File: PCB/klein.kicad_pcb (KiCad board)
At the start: 2 copper layers, 147.9 x 97.2 mm, 86 parts, among them J1 Conn_01x12, J2 Haptic Buzz, J3 Conn_01x04, J5 OLED-128x64, SW1 MX_SW_HS, SW10 MX_SW_HS, SW11 MX_SW_HS, SW12 MX_SW_HS, SW13 MX_SW_HS, SW14 MX_SW_HS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

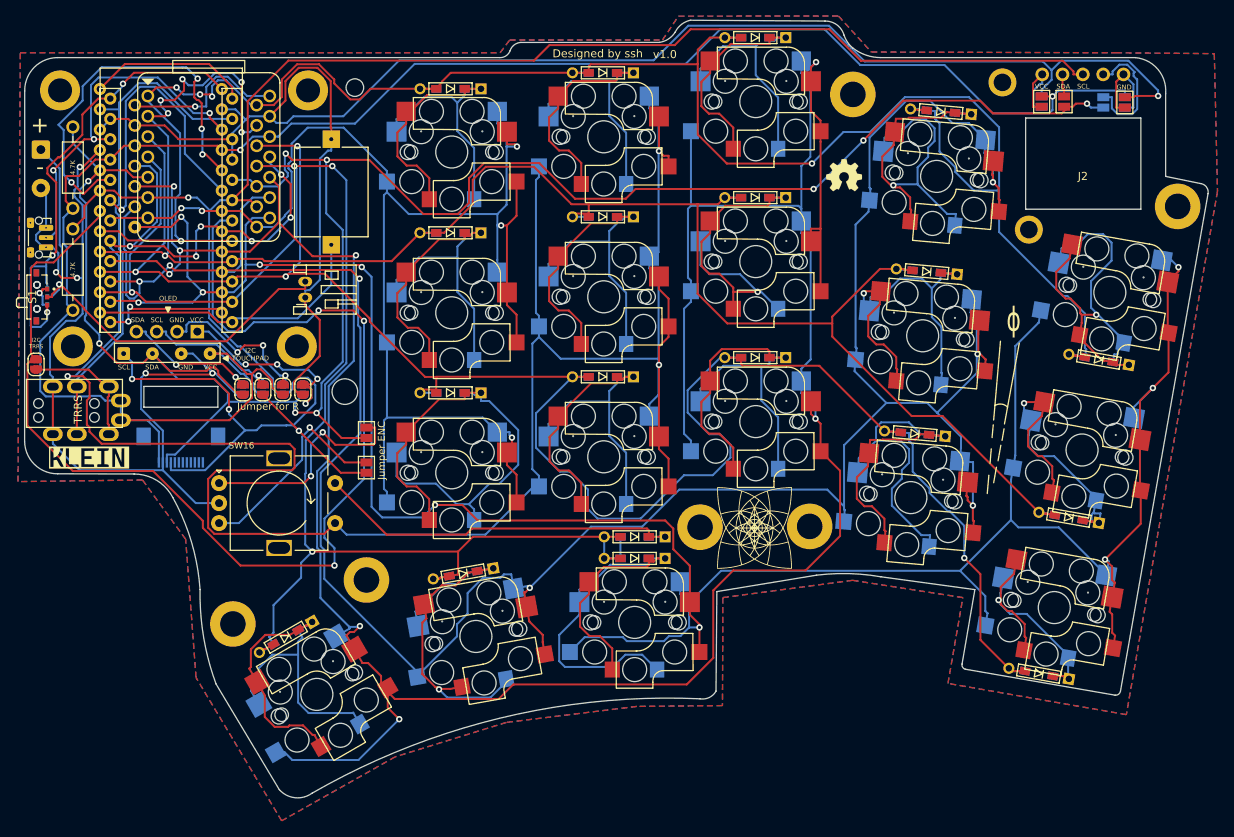
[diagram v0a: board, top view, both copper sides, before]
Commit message: Fix PCB Encoder Routes (Typo in Schematic) and IBOM project name fix
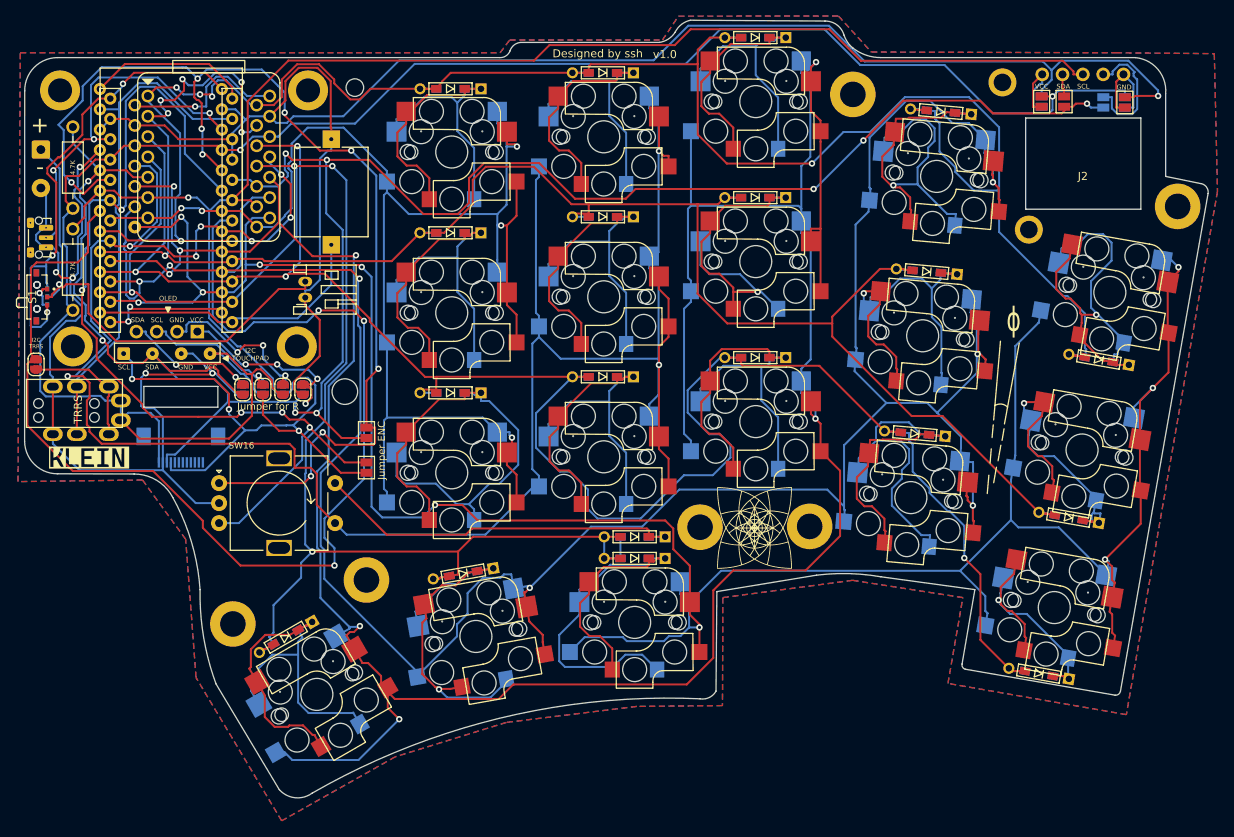
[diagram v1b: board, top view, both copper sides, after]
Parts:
- removed REF01, REF02: OSHW-Logo_5.7x6mm_SilkScreen, Symbol:OSHW-Logo_5.7x6mm_SilkScreen
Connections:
- U2 pad 19: ENCB -> ENC_B
- U2 pad 20: ENCA -> ENC_A
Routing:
- net ENC_A: track 28.2 -> 139.9 mm, vias 2 -> 9
- net ENC_B: track 27.0 -> 117.9 mm, vias 1 -> 5
- net ENCA: track 49.5 -> 0.00 mm, vias 4 -> 0
- net ENCB: track 36.6 -> 0.00 mm, vias 1 -> 0
- net COL 1: track 307.8 -> 286.5 mm
- net VCC_3V3: track 243.2 -> 248.0 mm
- net Net-(B1-Pad1): track 60.4 -> 62.8 mm
- net RX: track 146.9 -> 148.7 mm
- net SCL: track 249.3 -> 250.8 mm
- net SDA: track 267.9 -> 269.1 mm
- net GND: track 332.7 -> 333.4 mm
